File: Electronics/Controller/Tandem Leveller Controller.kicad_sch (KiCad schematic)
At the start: 4 parts, among them J1 Conn_01x02, U1 TEENSY 4.0

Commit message: Removed JLCPCB part numbers for Teensy and BNO085 connectors. Added JLCPCB part number for 4.7uF capacitor. Generated JLCPCB manufacturing files for all boards.
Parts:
- U1: LCSC C2897377 -> (none)
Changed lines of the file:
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@@
       (effects (font (size 1.27 1.27)) hide)
     )
-    (property "LCSC" "C2897377" (at 83.185 173.355 0)
+    (property "LCSC" "" (at 83.185 173.355 0)
       (effects (font (size 1.27 1.27)) hide)
     )

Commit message: Added fiducials to all boards.
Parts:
- added FID1, FID2, FID3: Fiducial, Fiducial:Fiducial_0.5mm_Mask1mm, symbol Mechanical:Fiducial
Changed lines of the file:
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@@
   (title_block
     (title "Tandem Leveller Controller")
-    (date "2025-03-11")
+    (date "2025-03-13")
     (rev "V1.0")
     (company "(C) andy@britishideas.com 2025")
@@
     (effects (font (size 1.27 1.27)) (justify left bottom))
   )
+  (symbol (lib_id "Mechanical:Fiducial") (at 149.225 188.595 0) (unit 1)
+    (in_bom yes) (on_board yes) (dnp no) (fields_autoplaced)
+    (property "Reference" "FID2" (at 151.765 187.325 0)
+      (effects (font (size 1.27 1.27)) (justify left))
+    )
+    (property "Value" "Fiducial" (at 151.765 189.865 0)
+      (effects (font (size 1.27 1.27)) (justify left))
+    )
+    (property "Footprint" "Fiducial:Fiducial_0.5mm_Mask1mm" (at 149.225 188.595 0)
+      (effects (font (size 1.27 1.27)) hide)
+    )
+    (property "Datasheet" "~" (at 149.225 188.595 0)
+      (effects (font (size 1.27 1.27)) hide)
+    )
+    (instances
+      (project "Tandem Leveller Controller"
+        (path "/56ffd1a6-bbed-43b6-8aa8-f23f49f76448"
+          (reference "FID2") (unit 1)
+        )
+      )
+    )
+  )
   (symbol (lib_id "Connector_Generic:Conn_01x02") (at 98.425 43.18 180) (unit 1)
     (in_bom yes) (on_board yes) (dnp no)
@@
     )
   )
+  (symbol (lib_id "Mechanical:Fiducial") (at 137.16 188.595 0) (unit 1)
+    (in_bom yes) (on_board yes) (dnp no) (fields_autoplaced)
+    (property "Reference" "FID1" (at 139.7 187.325 0)
+      (effects (font (size 1.27 1.27)) (justify left))
+    )
+    (property "Value" "Fiducial" (at 139.7 189.865 0)
+      (effects (font (size 1.27 1.27)) (justify left))
+    )
+    (property "Footprint" "Fiducial:Fiducial_0.5mm_Mask1mm" (at 137.16 188.595 0)
+      (effects (font (size 1.27 1.27)) hide)
+    )
+    (property "Datasheet" "~" (at 137.16 188.595 0)
+      (effects (font (size 1.27 1.27)) hide)
+    )
+    (instances
+      (project "Tandem Leveller Controller"
+        (path "/56ffd1a6-bbed-43b6-8aa8-f23f49f76448"
+          (reference "FID1") (unit 1)
+        )
+      )
+    )
+  )
   (symbol (lib_id "Device:LED") (at 195.58 33.655 90) (unit 1)
     (in_bom yes) (on_board yes) (dnp no) (fields_autoplaced)
@@
         )
       )
+    )
+  )
+  (symbol (lib_id "Mechanical:Fiducial") (at 161.29 188.595 0) (unit 1)
+    (in_bom yes) (on_board yes) (dnp no) (fields_autoplaced)
+    (property "Reference" "FID3" (at 163.83 187.325 0)
+      (effects (font (size 1.27 1.27)) (justify left))
+    )
+    (property "Value" "Fiducial" (at 163.83 189.865 0)
+      (effects (font (size 1.27 1.27)) (justify left))
+    )
+    (property "Footprint" "Fiducial:Fiducial_0.5mm_Mask1mm" (at 161.29 188.595 0)
+      (effects (font (size 1.27 1.27)) hide)
+    )
+    (property "Datasheet" "~" (at 161.29 188.595 0)
+      (effects (font (size 1.27 1.27)) hide)
+    )
+    (instances
+      (project "Tandem Leveller Controller"
+        (path "/56ffd1a6-bbed-43b6-8aa8-f23f49f76448"
+          (reference "FID3") (unit 1)
+        )
+      )

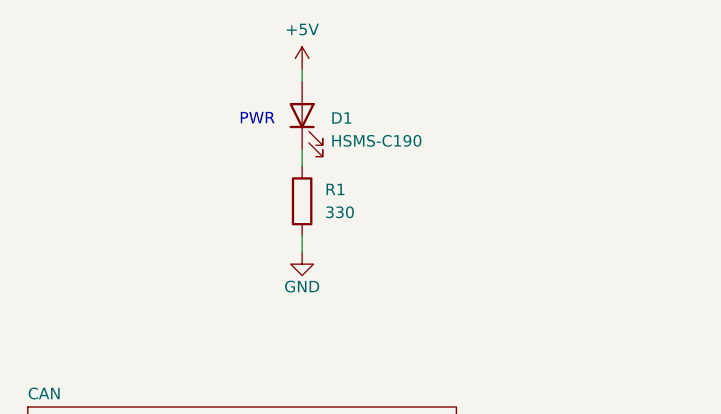
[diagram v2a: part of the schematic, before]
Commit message: Changed four way screw block, USB type A connectors, 33uH inductor and 24MHz crystal to use parts that JLCPCB has in stock.
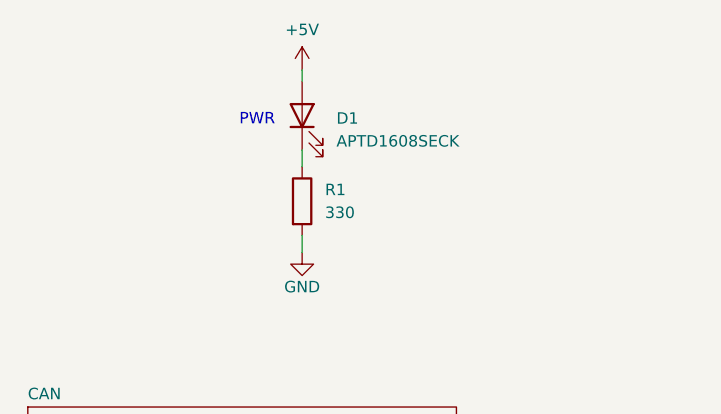
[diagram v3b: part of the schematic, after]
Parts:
- D1: value HSMS-C190 -> APTD1608SECK; LCSC (none) -> C5879220; manf# HSMS-C190 -> APTD1608SECK
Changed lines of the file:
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@@
   (title_block
     (title "Tandem Leveller Controller")
-    (date "2025-03-13")
+    (date "2025-03-18")
     (rev "V1.0")
     (company "(C) andy@britishideas.com 2025")
@@
   (symbol (lib_id "Device:LED") (at 195.58 33.655 90) (unit 1)
     (in_bom yes) (on_board yes) (dnp no) (fields_autoplaced)
-    (property "Reference" "D1" (at 198.755 33.9724 90)
+    (property "Reference" "D1" (at 199.39 33.9725 90)
       (effects (font (size 1.27 1.27)) (justify right))
     )
-    (property "Value" "HSMS-C190" (at 198.755 36.5124 90)
+    (property "Value" "APTD1608SECK" (at 199.39 36.5125 90)
       (effects (font (size 1.27 1.27)) (justify right))
     )
@@
       (effects (font (size 1.27 1.27)) hide)
     )
-    (property "manf#" "HSMS-C190" (at 195.58 33.655 90)
-      (effects (font (size 1.27 1.27)) hide)
-    )
-    (property "LCSC" "" (at 195.58 33.655 0)
-      (effects (font (size 1.27 1.27)) hide)
-    )
+    (property "manf#" "APTD1608SECK" (at 195.58 33.655 90)
+      (effects (font (size 1.27 1.27)) hide)
+    )
+    (property "LCSC" "C5879220" (at 195.58 33.655 0)
+      (effects (font (size 1.27 1.27)) hide)
+    )
